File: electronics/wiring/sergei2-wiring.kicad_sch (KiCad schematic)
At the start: 31 parts, among them J1 6i25 port 1, J2 6i25 port 2, M1 UGRMEM, M2 UGRMEM, M3 MY1016, M4 Spindle, SW1 ESTOP, SW2 Mode switch, SW3 Run, SW4 Door closed, SW5 Pause, U1 Power_control_PCB

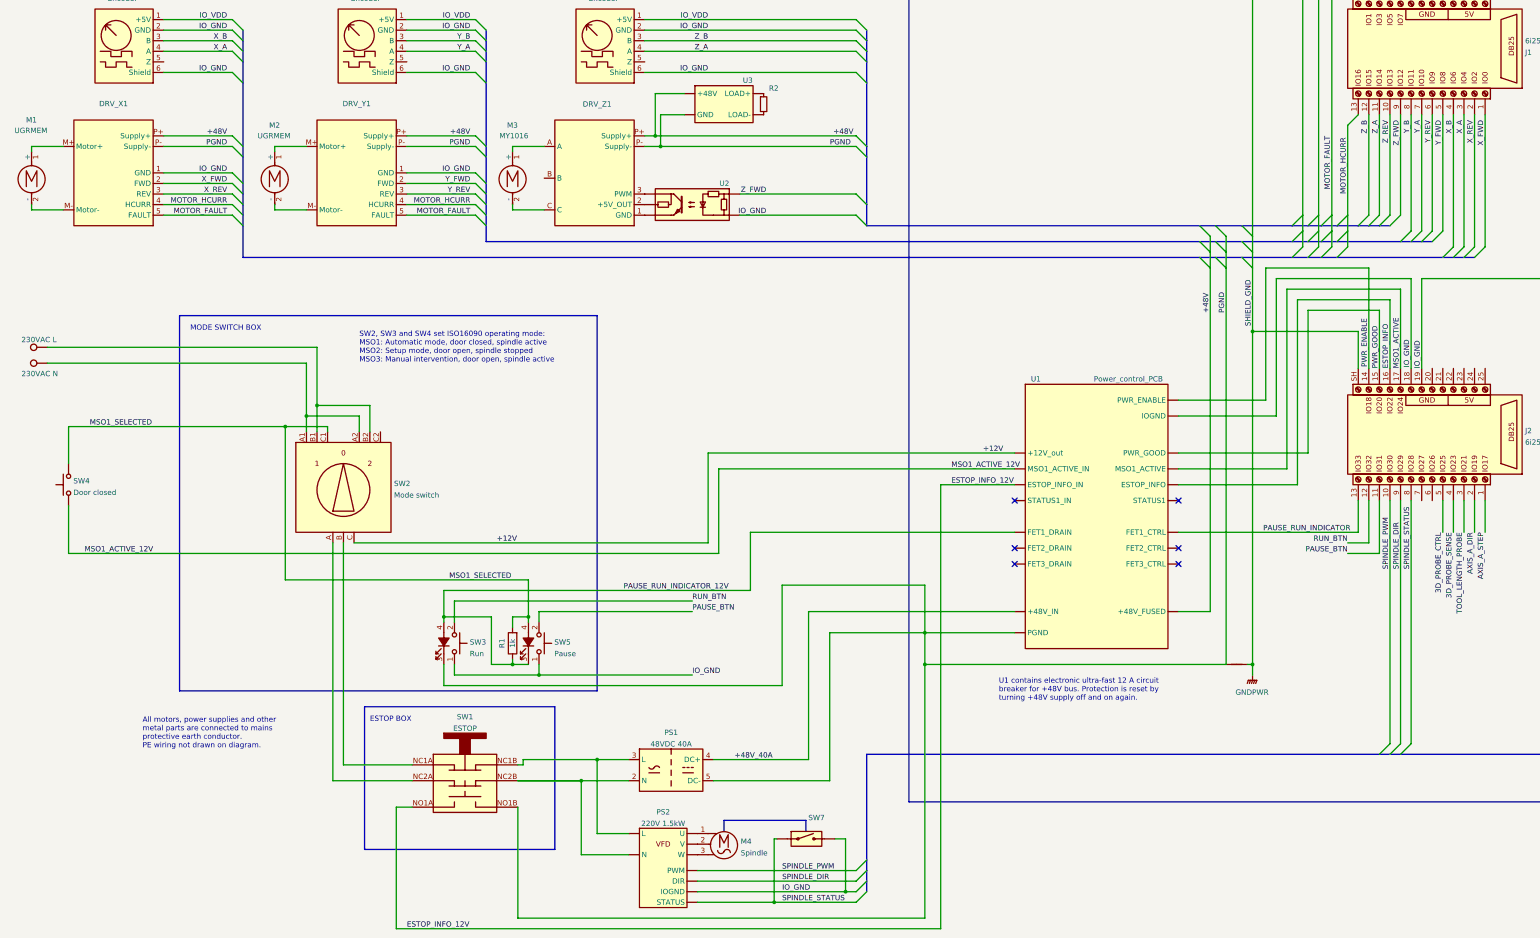
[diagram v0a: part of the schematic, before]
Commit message: Update parts list and wiring diagram
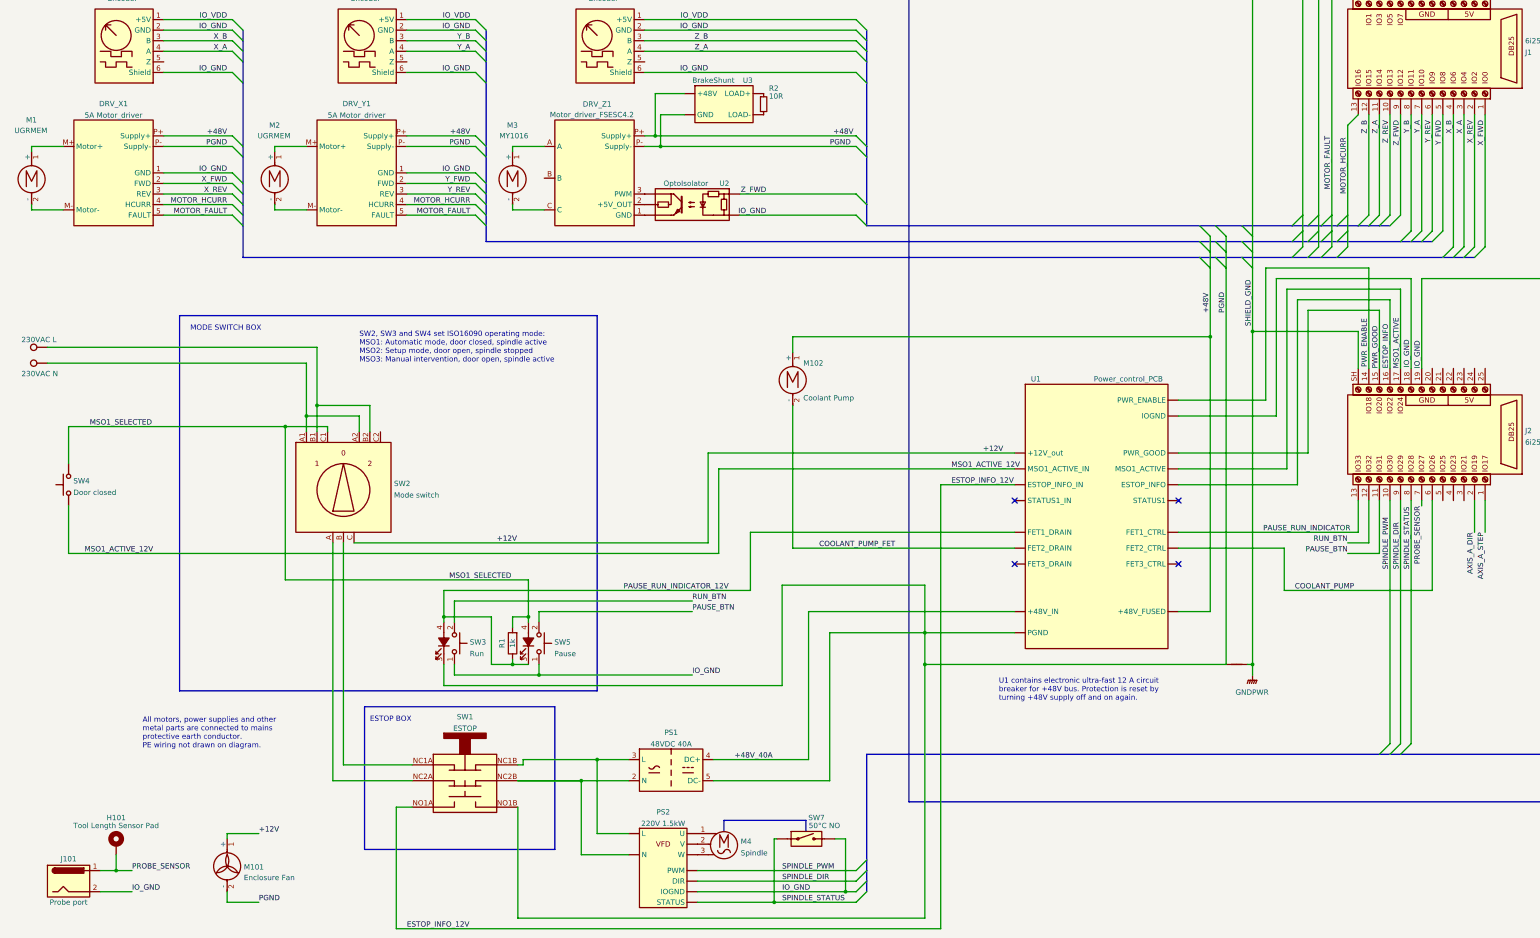
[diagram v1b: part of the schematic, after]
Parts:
- added H101: Tool Length Sensor Pad, symbol Mechanical:MountingHole_Pad
- added J101: Probe port, symbol Connector:Jack-DC
- added M101: Enclosure Fan, symbol Motor:Fan
- added M102: Coolant Pump, symbol Motor:Motor_DC
- DRV_X1, DRV_Y1: value (none) -> 5A Motor_driver
- DRV_Z1: value (none) -> Motor_driver_FSESC4.2
- R2: value (none) -> 10R
- SW7: value (none) -> 50°C NO
- U2: value (none) -> OptoIsolator
- U3: value (none) -> BrakeShunt
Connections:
- net +12V: now also M101.1 (+)
- net +48V: now also M102.1 (+)
- net IO_GND: now also J101.2
- net PGND: now also M101.2 (-)
- net COOLANT_PUMP: now reaches J2.6
- net COOLANT_PUMP: now also U1. (STATUS1_IN)
- net PROBE_SENSOR: now reaches J2.7
- net PROBE_SENSOR: now also H101.1, J101.1
- net 3D_PROBE_CTRL: no longer names the net of J2.5
- net 3D_PROBE_SENSE: no longer names the net of J2.4
- net TOOL_LENGTH_PROBE: no longer names the net of J2.3
- new net COOLANT_PUMP_FET: M102.2 (-), U1. (STATUS1_IN)
- no-connect marks 6 -> 4

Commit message: Update probe port in wiring diagram.
Switching to 3.5mm jack to provide power to 3D probe.
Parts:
- removed J101: Probe port, symbol Connector:Jack-DC
- added J?: Probe port, symbol Connector:AudioJack3_SwitchTR
- added R?: 470, symbol Device:R
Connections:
- net IO_GND: now also J?.S, R?.2
- net IO_VDD: now also J2.23, J?.T
- net PROBE_SENSOR: now also J?.R
- net PROBE_CONNECTED: now reaches J2.5
- net PROBE_CONNECTED: now also J?.TN, R?.1
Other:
- moved on the sheet: H101

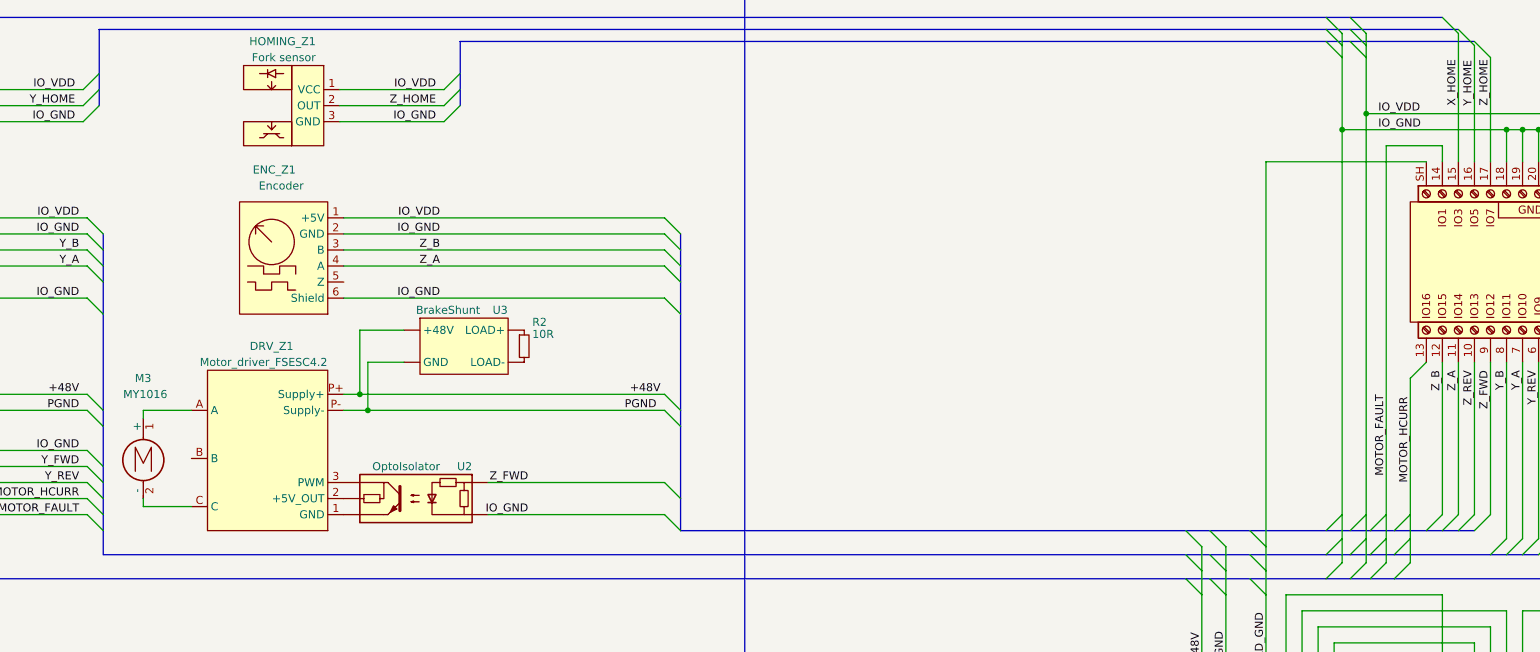
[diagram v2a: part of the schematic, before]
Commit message: Update wiring diagram
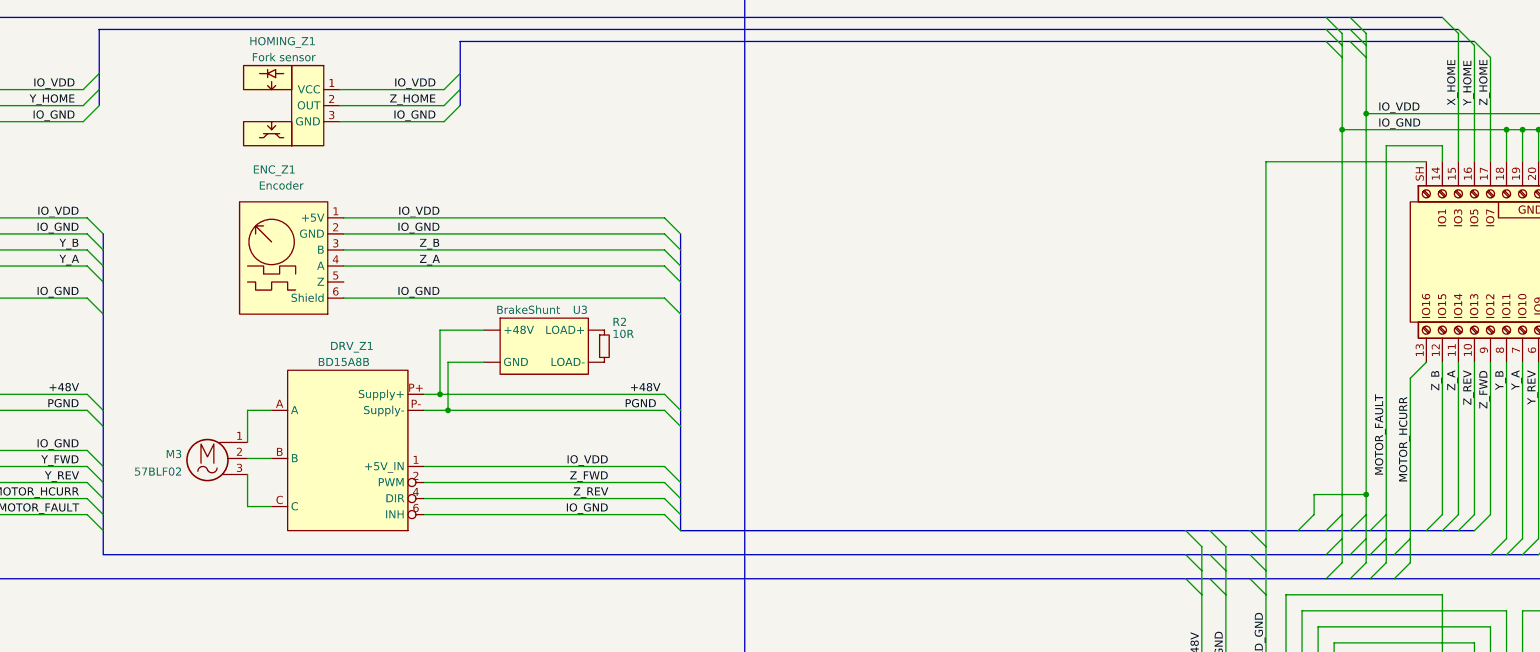
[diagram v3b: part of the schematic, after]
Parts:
- removed M3: MY1016, symbol Motor:Motor_DC
- removed U2: OptoIsolator, symbol sergei2_wiring:OptoIsolator
- added M3: 57BLF02, symbol sergei2_wiring:Motor_AC_3PHASE
- DRV_Z1: value Motor_driver_FSESC4.2 -> BD15A8B; symbol sergei2_wiring:Motor_driver_FSESC -> sergei2_wiring:Motor_driver_AMC
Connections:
- net IO_GND: now also DRV_Z1.6 (INH)
- net IO_VDD: now also DRV_Z1.1 (+5V_IN)
- net Z_FWD: now also DRV_Z1.2 (PWM)
- net Z_REV: now also DRV_Z1.4 (DIR)
- net at DRV_Z1.A: now also M3.1
- net at DRV_Z1.B: now also M3.2
- net at DRV_Z1.C: now also M3.3
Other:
- moved on the sheet: R2, U3
